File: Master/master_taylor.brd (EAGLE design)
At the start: 82.4 x 82.4 mm, 50 parts, among them J1 ISP, K1 653002114822, K2 653002114822, K3 653002114822, K4 653002114822, U1 ATMEGA128RFA1, U2 TPS73633-DBVT, U3 ULN2003ADR, Y1 16MHz, Y2 32.768kHz

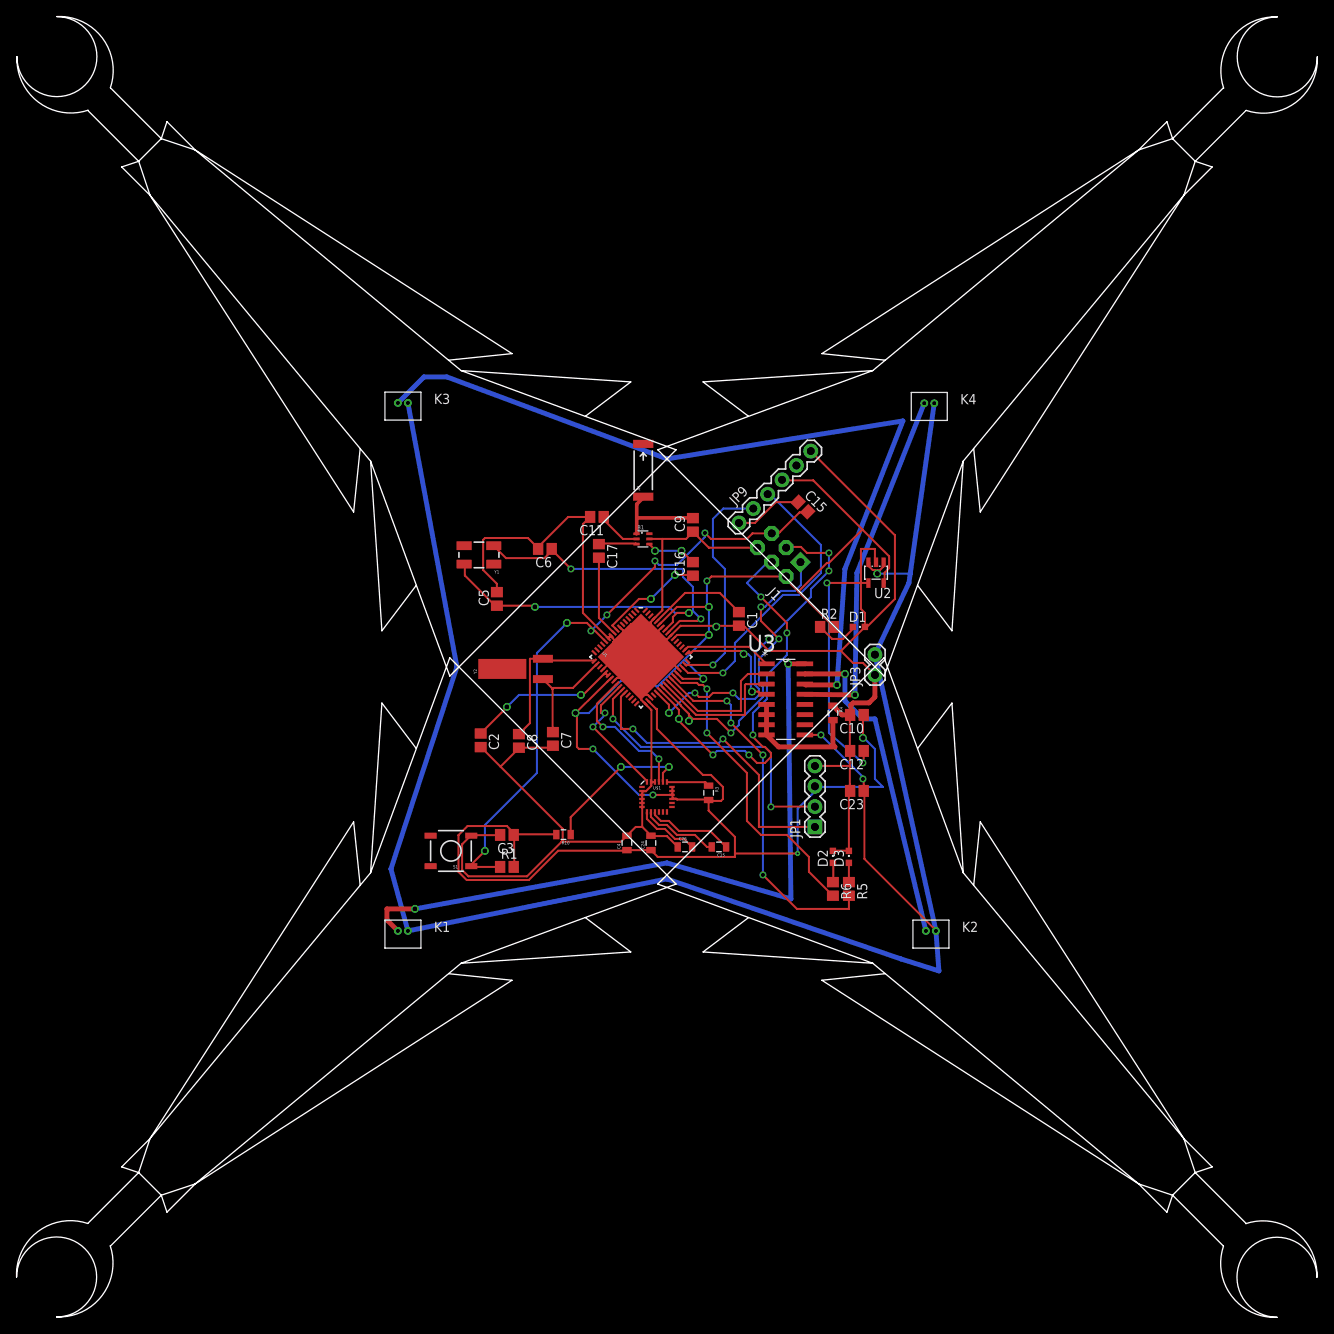
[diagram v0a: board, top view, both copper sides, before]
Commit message: Fixed some minor ERC errors
Adjusted wing fins.
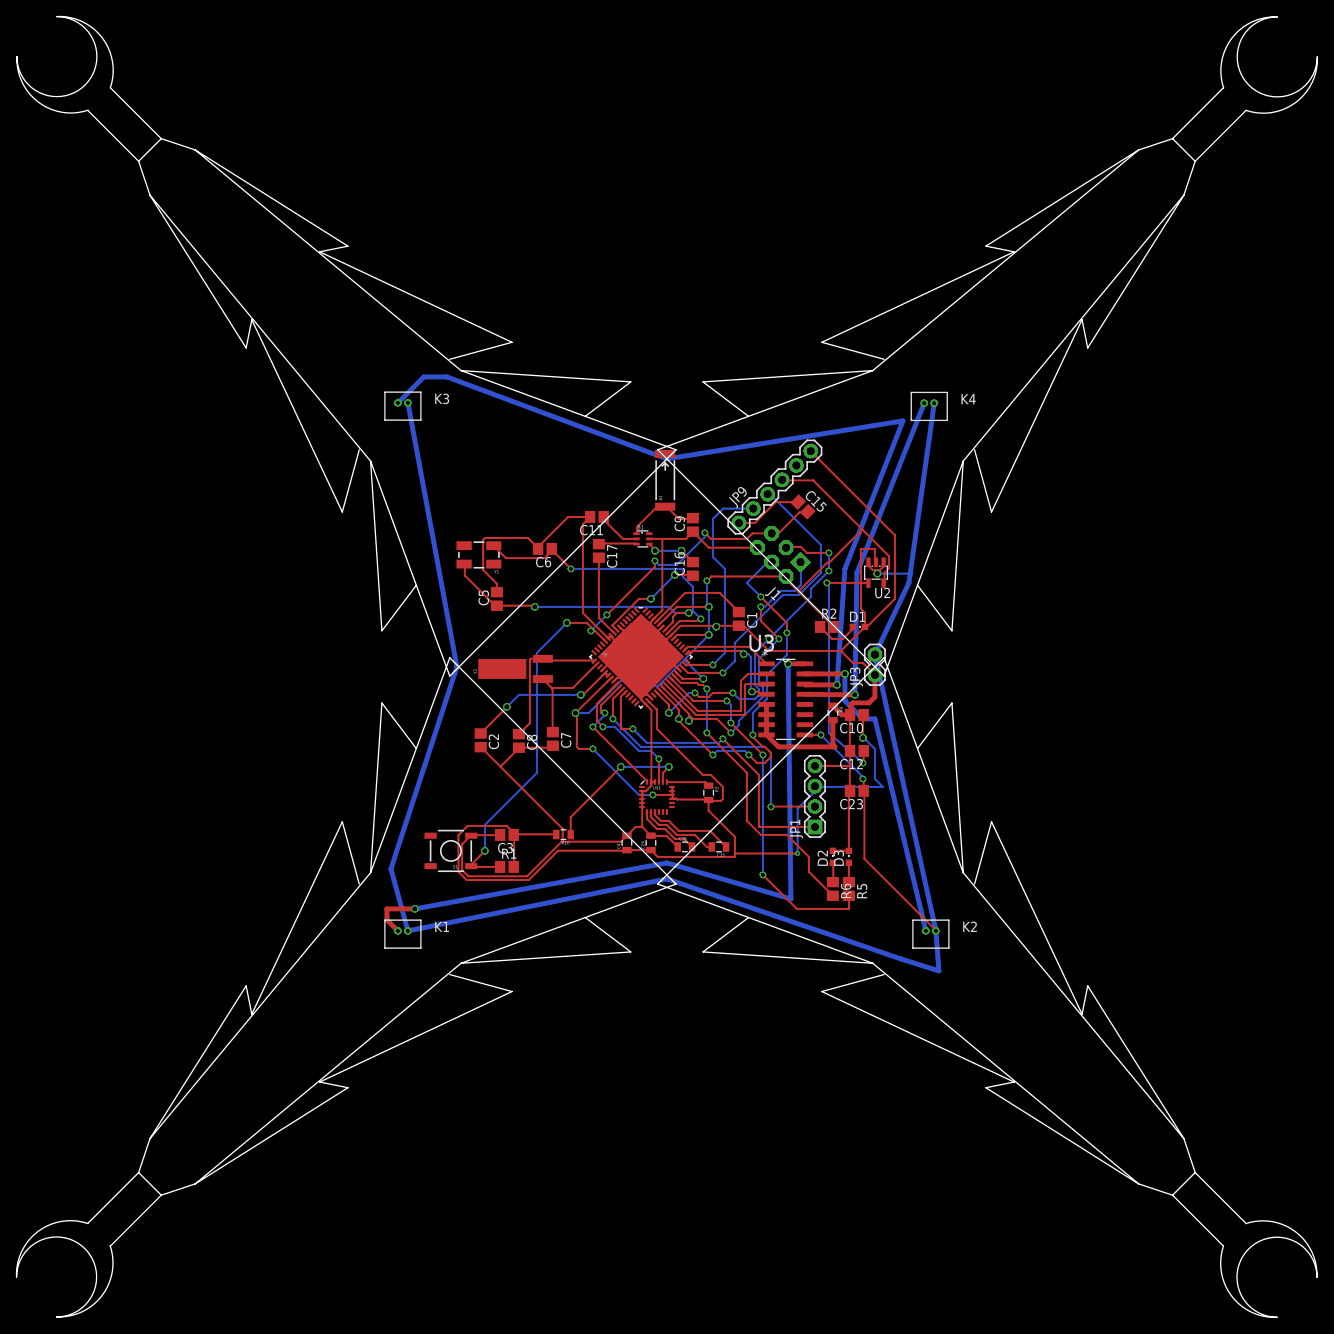
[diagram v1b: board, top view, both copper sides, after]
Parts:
- moved A1 3.02 mm to (-0.21, 23.3)
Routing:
- net RFANT: track 12.1 -> 9.63 mm
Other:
- outline, holes or cut-outs redrawn
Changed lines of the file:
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@@
 </autorouter>
 <elements>
-<element name="A1" library="SparkFun-RF" package="ANTENNA-CHIP5" value="ANTENNA2SMD5" x="-2.96" y="24.58" rot="R90"/>
+<element name="A1" library="SparkFun-RF" package="ANTENNA-CHIP5" value="ANTENNA2SMD5" x="-0.21" y="23.33" rot="R90"/>
 <element name="B1" library="SparkFun-RF" package="BALUN" value="748421245" x="-3" y="16" rot="R270"/>
 <element name="C1" library="resistor" package="C0805" value="1uF" x="9" y="6" rot="R270"/>
@@
 <contactref element="C9" pad="2"/>
 <contactref element="A1" pad="FEED"/>
-<wire x1="-3.7719" y1="20.3454" x2="-3.7719" y2="18.6309" width="0.4572" layer="1"/>
-<wire x1="-3.7719" y1="18.6309" x2="-3.7719" y2="16.6878" width="0.4572" layer="1"/>
-<wire x1="-2.8575" y1="21.2598" x2="-3.7719" y2="20.3454" width="0.4572" layer="1"/>
-<wire x1="-3.7719" y1="16.6878" x2="-3.8" y2="16.65" width="0.4572" layer="1"/>
-<wire x1="-2.8575" y1="21.2598" x2="-2.96" y2="21.278" width="0.4572" layer="1"/>
-<wire x1="-3.7719" y1="18.6309" x2="3.2004" y2="18.6309" width="0.4572" layer="1"/>
-<wire x1="3.2004" y1="18.6309" x2="3.25" y2="18.6" width="0.4572" layer="1"/>
+<wire x1="1.5" y1="18.5" x2="0" y2="20" width="0.254" layer="1"/>
+<wire x1="3.25" y1="18.5" x2="1.5" y2="18.5" width="0.254" layer="1"/>
+<wire x1="0" y1="20" x2="-0.21" y2="20.028" width="0.254" layer="1"/>
+<wire x1="3.25" y1="18.5" x2="3.25" y2="18.6" width="0.254" layer="1"/>
+<wire x1="-3.75" y1="17.5" x2="-3.75" y2="16.75" width="0.254" layer="1"/>
+<wire x1="-1.25" y1="20" x2="-3.75" y2="17.5" width="0.254" layer="1"/>
+<wire x1="-0.25" y1="20" x2="-1.25" y2="20" width="0.254" layer="1"/>
+<wire x1="-3.75" y1="16.75" x2="-3.8" y2="16.65" width="0.254" layer="1"/>
+<wire x1="-0.25" y1="20" x2="-0.21" y2="20.028" width="0.254" layer="1"/>
 </signal>
 <signal name="RESET">

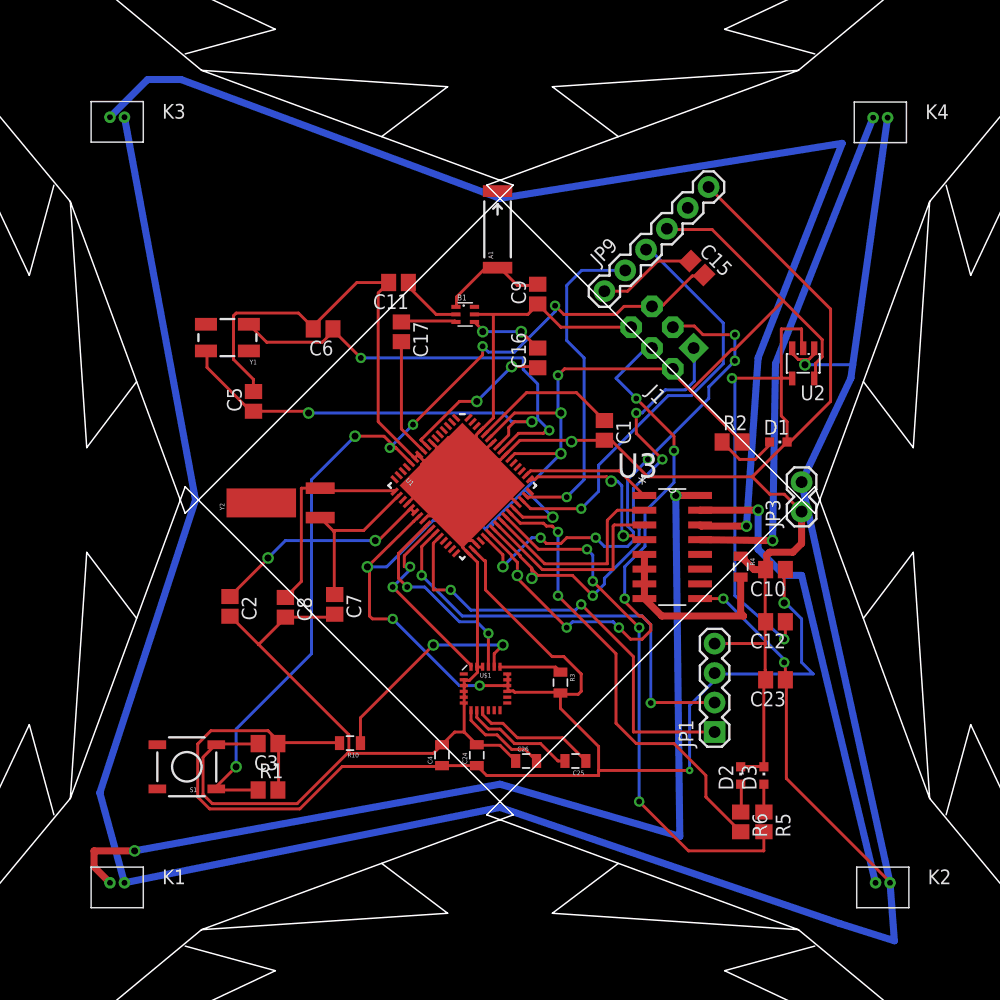
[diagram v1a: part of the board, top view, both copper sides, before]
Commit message: Fixed DRC and ERC errors
The downside to handrouting.
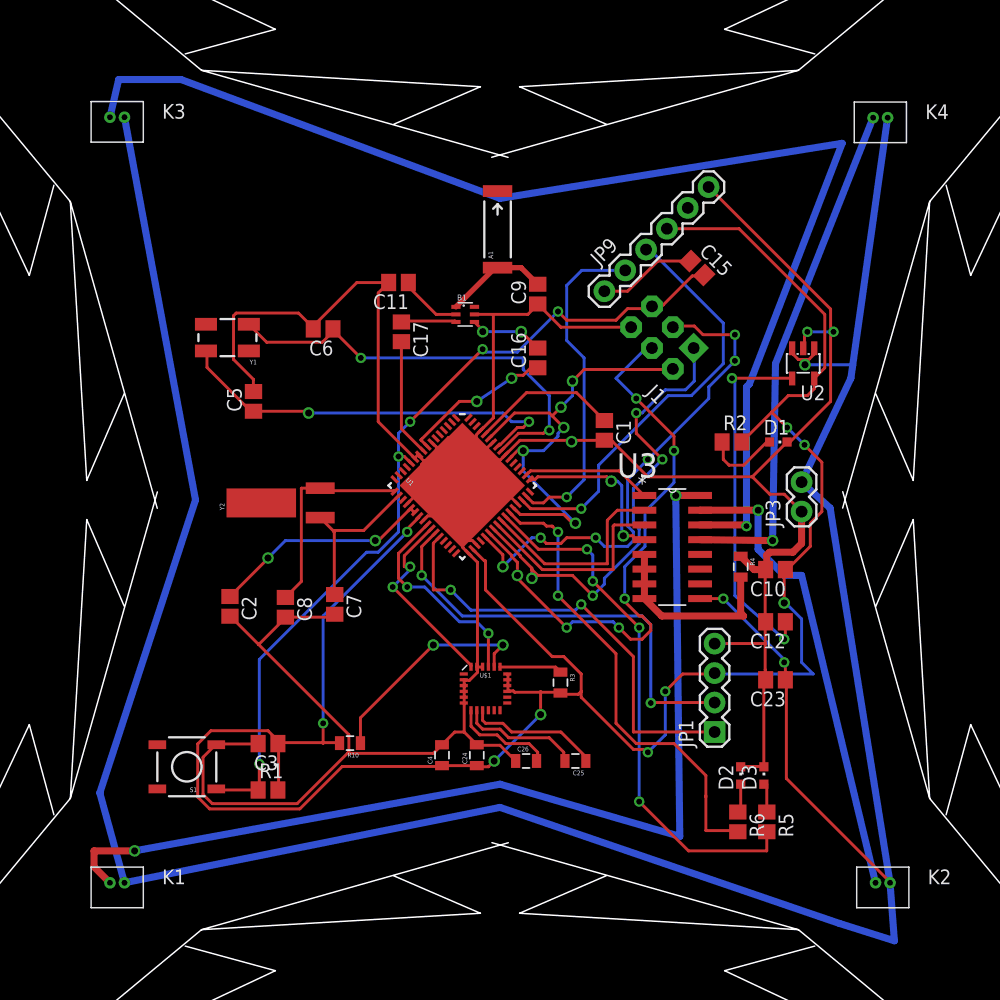
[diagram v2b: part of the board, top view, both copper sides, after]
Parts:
- moved R5 0.25 mm to (23.0, -27.8)
- moved R6 0.25 mm to (20.5, -27.8)
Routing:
- net 3.3V: track 252.4 -> 233.4 mm, vias 9 -> 14
- net GND: track 305.7 -> 296.3 mm, vias 1 -> 3
- net RESET: track 80.4 -> 74.2 mm, vias 6 -> 5
- net PB7: track 39.2 -> 40.7 mm
- net N$31: track 105.1 -> 106.6 mm
- net N$2: track 5.49 -> 6.89 mm
- net N$20: track 7.97 -> 8.91 mm
- net N$3: track 35.7 -> 34.8 mm
- net N$21: track 9.78 -> 10.5 mm
- net VBAT: track 251.6 -> 252.3 mm
- net N$22: track 10.9 -> 11.6 mm
- net RFANT: track 9.63 -> 9.04 mm
- net N$8: track 2.40 -> 2.98 mm
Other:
- board size 82.4 x 82.4 mm -> 82 x 82 mm

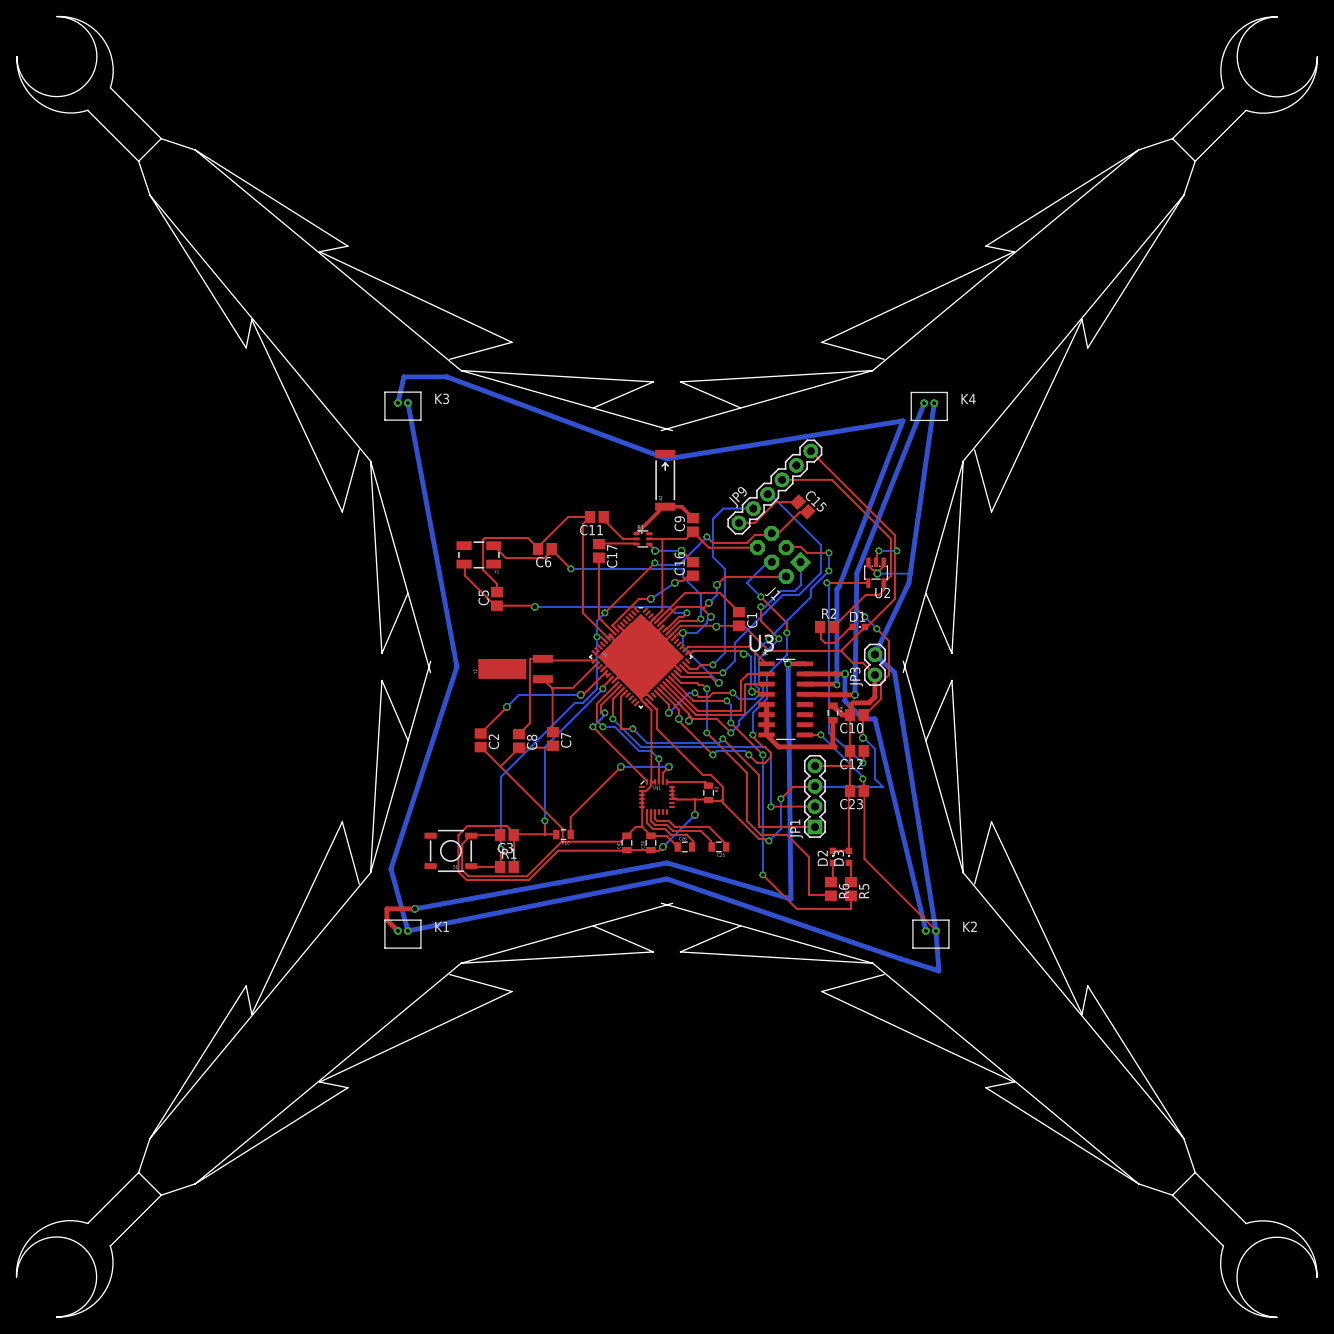
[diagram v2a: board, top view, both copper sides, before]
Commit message: IMU has name and value
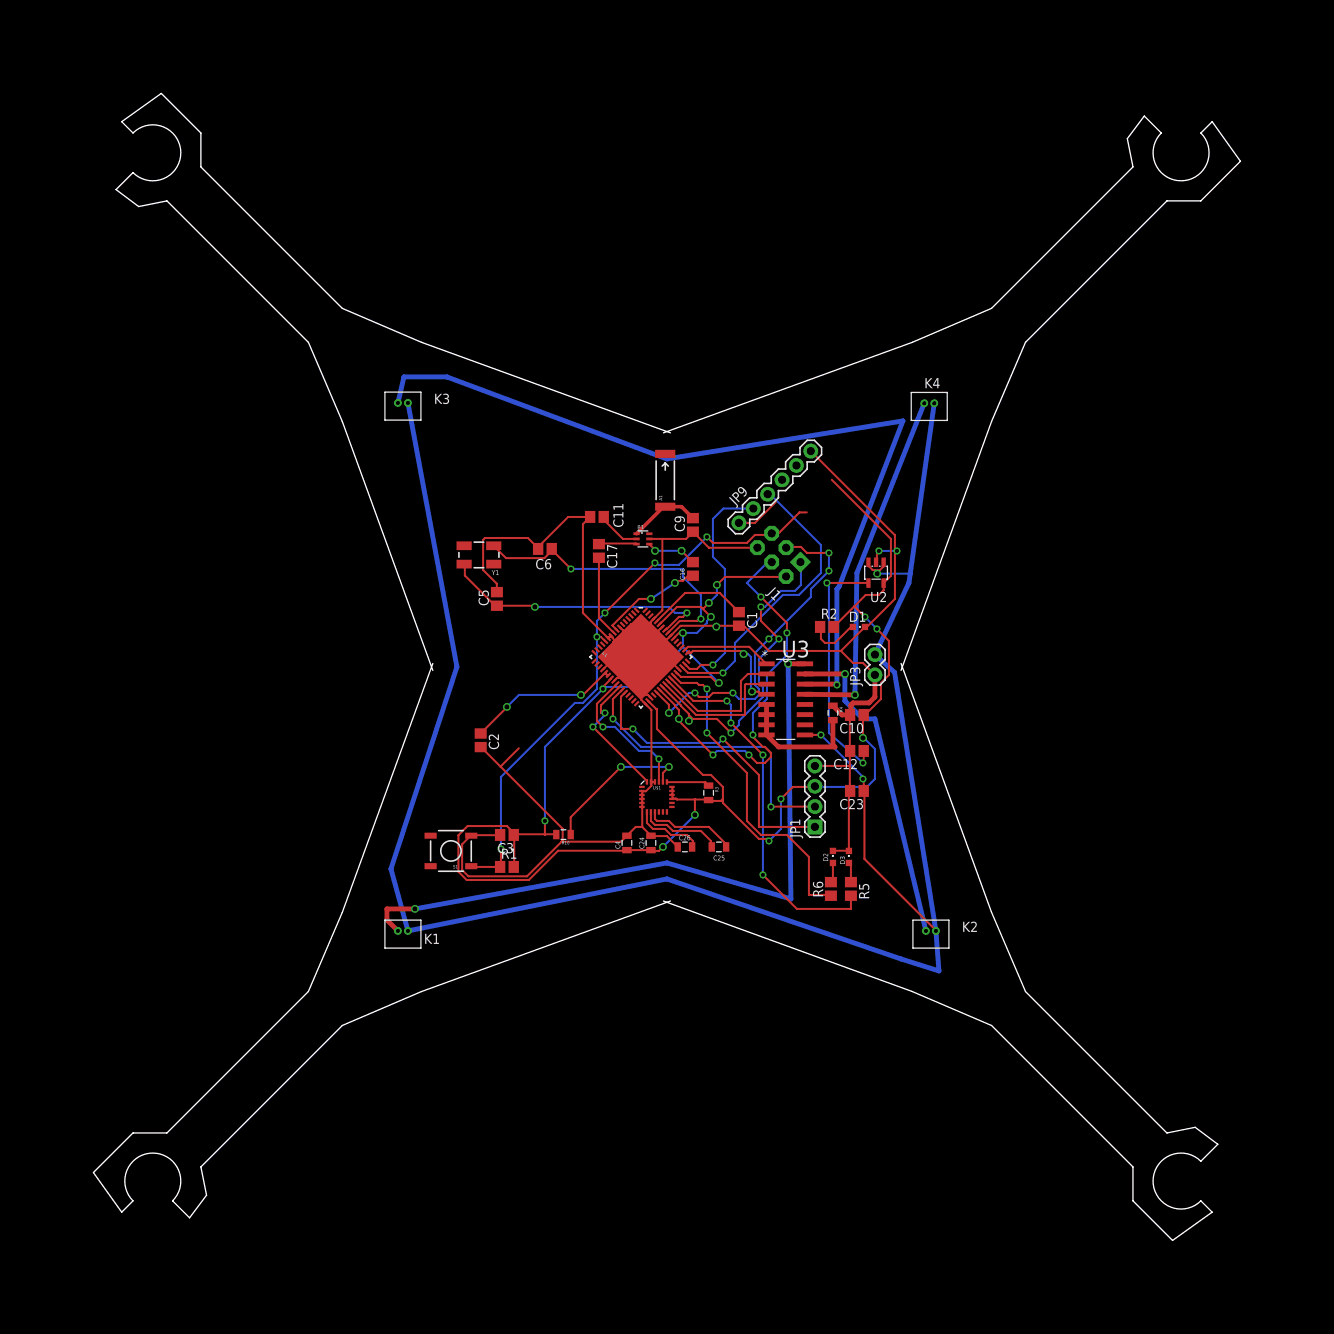
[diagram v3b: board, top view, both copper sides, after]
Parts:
- removed C15: 0.1uF, resistor:C0805
- removed C7, C8: 12pF, resistor:C0805
- removed Y2: 32.768kHz, SparkFun-FreqCtrl:CRYSTAL-32KHZ-SMD
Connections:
- removed net N$5: C7.1, U1.18, Y2.X1
- removed net N$6: C8.1, U1.17, Y2.X2
- new net N$14: J1.2
- new net N$9: JP9.VCC
- net 3.3V: no longer J1.2, JP9.VCC
- net DTR: no longer C15.1
- net GND: no longer C7.2, C8.2
- net RESET: no longer C15.2
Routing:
- net N$6: track 18.2 -> 0.00 mm
- net N$5: track 14.0 -> 0.00 mm
- net GND: track 296.3 -> 291.9 mm
- net 3.3V: track 233.4 -> 237.5 mm
- net DTR: track 8.48 -> 5.68 mm
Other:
- board size 82 x 82 mm -> 72.1 x 69.3 mm
